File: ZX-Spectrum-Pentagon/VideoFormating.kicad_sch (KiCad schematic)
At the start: 10 parts

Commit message: prepare for pcb
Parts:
- RVF1: value (none) -> 4.7kOm; footprint (none) -> Resistor_SMD:R_0805_2012Metric_Pad1.20x1.40mm_HandSolder
- SWIO2: value (none) -> SW_Push_DPDT; footprint (none) -> Button_Switch_THT:SW_E-Switch_EG2219_DPDT_Angled
- U35, U36, U40: value (none) -> 74HC574; footprint (none) -> Package_DIP:DIP-20_W7.62mm
- U37, U38: value (none) -> 74HC153; footprint (none) -> Package_DIP:DIP-16_W7.62mm
- U39: value (none) -> GAL16V8; footprint (none) -> Package_DIP:DIP-20_W7.62mm
- U41: value (none) -> 74HC166; footprint (none) -> Package_DIP:DIP-16_W7.62mm
- U9: value (none) -> 74HC86; footprint (none) -> Package_DIP:DIP-14_W7.62mm
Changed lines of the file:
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@@
     (in_bom yes) (on_board yes)
     (property "Reference" "U35" (id 0) (at 55.88 24.13 0))
-    (property "Value" "" (id 1) (at 55.88 52.07 0))
-    (property "Footprint" "" (id 2) (at 55.88 45.72 0)
+    (property "Value" "74HC574" (id 1) (at 55.88 52.07 0))
+    (property "Footprint" "Package_DIP:DIP-20_W7.62mm" (id 2) (at 55.88 45.72 0)
       (effects (font (size 1.27 1.27)) hide)
     )
@@
     (in_bom yes) (on_board yes)
     (property "Reference" "U36" (id 0) (at 78.74 26.67 0))
-    (property "Value" "" (id 1) (at 78.74 54.61 0))
-    (property "Footprint" "" (id 2) (at 78.74 48.26 0)
+    (property "Value" "74HC574" (id 1) (at 78.74 54.61 0))
+    (property "Footprint" "Package_DIP:DIP-20_W7.62mm" (id 2) (at 78.74 48.26 0)
       (effects (font (size 1.27 1.27)) hide)
     )
@@
     (in_bom yes) (on_board yes)
     (property "Reference" "U40" (id 0) (at 55.88 153.67 0))
-    (property "Value" "" (id 1) (at 55.88 181.61 0))
-    (property "Footprint" "" (id 2) (at 55.88 175.26 0)
+    (property "Value" "74HC574" (id 1) (at 55.88 181.61 0))
+    (property "Footprint" "Package_DIP:DIP-20_W7.62mm" (id 2) (at 55.88 175.26 0)
       (effects (font (size 1.27 1.27)) hide)
     )
@@
     (in_bom yes) (on_board yes)
     (property "Reference" "U41" (id 0) (at 82.55 151.13 0))
-    (property "Value" "" (id 1) (at 82.55 186.69 0))
-    (property "Footprint" "" (id 2) (at 82.55 184.15 0)
+    (property "Value" "74HC166" (id 1) (at 82.55 186.69 0))
+    (property "Footprint" "Package_DIP:DIP-16_W7.62mm" (id 2) (at 82.55 184.15 0)
       (effects (font (size 1.27 1.27)) hide)
     )
@@
     (in_bom yes) (on_board yes)
     (property "Reference" "U37" (id 0) (at 135.89 26.67 0))
-    (property "Value" "" (id 1) (at 135.89 59.69 0))
-    (property "Footprint" "" (id 2) (at 135.89 41.91 0)
+    (property "Value" "74HC153" (id 1) (at 135.89 59.69 0))
+    (property "Footprint" "Package_DIP:DIP-16_W7.62mm" (id 2) (at 135.89 41.91 0)
       (effects (font (size 1.27 1.27)) hide)
     )
@@
     (in_bom yes) (on_board yes)
     (property "Reference" "U38" (id 0) (at 135.89 72.39 0))
-    (property "Value" "" (id 1) (at 135.89 105.41 0))
-    (property "Footprint" "" (id 2) (at 135.89 87.63 0)
+    (property "Value" "74HC153" (id 1) (at 135.89 105.41 0))
+    (property "Footprint" "Package_DIP:DIP-16_W7.62mm" (id 2) (at 135.89 87.63 0)
       (effects (font (size 1.27 1.27)) hide)
     )
@@
     (in_bom yes) (on_board yes)
     (property "Reference" "U39" (id 0) (at 83.82 95.25 0))
-    (property "Value" "" (id 1) (at 83.82 123.19 0))
-    (property "Footprint" "" (id 2) (at 83.82 95.25 0)
+    (property "Value" "GAL16V8" (id 1) (at 83.82 123.19 0))
+    (property "Footprint" "Package_DIP:DIP-20_W7.62mm" (id 2) (at 83.82 95.25 0)
       (effects (font (size 1.27 1.27)) hide)
     )
@@
     (in_bom yes) (on_board yes)
     (property "Reference" "SWIO2" (id 0) (at 114.3 156.21 0))
-    (property "Value" "" (id 1) (at 114.3 156.3624 0)
-      (effects (font (size 1.27 1.27)) hide)
-    )
-    (property "Footprint" "" (id 2) (at 114.3 161.29 0)
+    (property "Value" "SW_Push_DPDT" (id 1) (at 114.3 156.3624 0)
+      (effects (font (size 1.27 1.27)) hide)
+    )
+    (property "Footprint" "Button_Switch_THT:SW_E-Switch_EG2219_DPDT_Angled" (id 2) (at 114.3 161.29 0)
       (effects (font (size 1.27 1.27)) hide)
     )
@@
       (effects (font (size 1.27 1.27)) (justify left))
     )
-    (property "Value" "" (id 1) (at 97.79 157.48 0)
+    (property "Value" "4.7kOm" (id 1) (at 97.79 157.48 0)
       (effects (font (size 1.27 1.27)) (justify left))
     )
-    (property "Footprint" "" (id 2) (at 104.902 153.67 90)
+    (property "Footprint" "Resistor_SMD:R_0805_2012Metric_Pad1.20x1.40mm_HandSolder" (id 2) (at 104.902 153.67 90)
       (effects (font (size 1.27 1.27)) hide)
     )
@@
     (in_bom yes) (on_board yes)
     (property "Reference" "U9" (id 0) (at 137.16 133.35 0))
-    (property "Value" "" (id 1) (at 137.16 140.97 0))
-    (property "Footprint" "" (id 2) (at 137.16 144.78 0)
-      (effects (font (size 1.27 1.27)) hide)
-    )
+    (property "Value" "74HC86" (id 1) (at 137.16 140.97 0))
+    (property "Footprint" "Package_DIP:DIP-14_W7.62mm" (id 2) (at 137.16 144.78 0)
+      (effects (font (size 1.27 1.27)) hide)
+    )

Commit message: clear annotate
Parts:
- renumbered RVF1 to RVF?, SWIO2 to SWIO?, U35 to U?, U36 to U?, U40 to U?, U41 to U?, U37 to U?, U38 to U?, U39 to U?, U9 to U?
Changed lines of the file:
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@@
   (symbol (lib_id "74IEC:74HC574") (at 55.88 38.1 0) (unit 1)
     (in_bom yes) (on_board yes)
-    (property "Reference" "U35" (id 0) (at 55.88 24.13 0))
+    (property "Reference" "U?" (id 0) (at 55.88 24.13 0))
     (property "Value" "74HC574" (id 1) (at 55.88 52.07 0))
     (property "Footprint" "Package_DIP:DIP-20_W7.62mm" (id 2) (at 55.88 45.72 0)
@@
   (symbol (lib_id "74IEC:74HC574") (at 78.74 40.64 0) (unit 1)
     (in_bom yes) (on_board yes)
-    (property "Reference" "U36" (id 0) (at 78.74 26.67 0))
+    (property "Reference" "U?" (id 0) (at 78.74 26.67 0))
     (property "Value" "74HC574" (id 1) (at 78.74 54.61 0))
     (property "Footprint" "Package_DIP:DIP-20_W7.62mm" (id 2) (at 78.74 48.26 0)
@@
   (symbol (lib_id "power:GND") (at 68.58 57.15 0) (unit 1)
     (in_bom yes) (on_board yes)
-    (property "Reference" "#PWR0157" (id 0) (at 68.58 63.5 0)
+    (property "Reference" "#PWR?" (id 0) (at 68.58 63.5 0)
       (effects (font (size 1.27 1.27)) hide)
     )
@@
   (symbol (lib_id "74IEC:74HC574") (at 55.88 167.64 0) (unit 1)
     (in_bom yes) (on_board yes)
-    (property "Reference" "U40" (id 0) (at 55.88 153.67 0))
+    (property "Reference" "U?" (id 0) (at 55.88 153.67 0))
     (property "Value" "74HC574" (id 1) (at 55.88 181.61 0))
     (property "Footprint" "Package_DIP:DIP-20_W7.62mm" (id 2) (at 55.88 175.26 0)
@@
   (symbol (lib_id "74IEC:74HC166") (at 82.55 168.91 0) (unit 1)
     (in_bom yes) (on_board yes)
-    (property "Reference" "U41" (id 0) (at 82.55 151.13 0))
+    (property "Reference" "U?" (id 0) (at 82.55 151.13 0))
     (property "Value" "74HC166" (id 1) (at 82.55 186.69 0))
     (property "Footprint" "Package_DIP:DIP-16_W7.62mm" (id 2) (at 82.55 184.15 0)
@@
   (symbol (lib_id "power:GND") (at 71.12 186.69 0) (unit 1)
     (in_bom yes) (on_board yes)
-    (property "Reference" "#PWR0155" (id 0) (at 71.12 193.04 0)
+    (property "Reference" "#PWR?" (id 0) (at 71.12 193.04 0)
       (effects (font (size 1.27 1.27)) hide)
     )
@@
   (symbol (lib_id "74IEC:74XX153") (at 135.89 43.18 0) (unit 1)
     (in_bom yes) (on_board yes)
-    (property "Reference" "U37" (id 0) (at 135.89 26.67 0))
+    (property "Reference" "U?" (id 0) (at 135.89 26.67 0))
     (property "Value" "74HC153" (id 1) (at 135.89 59.69 0))
     (property "Footprint" "Package_DIP:DIP-16_W7.62mm" (id 2) (at 135.89 41.91 0)
@@
   (symbol (lib_id "74IEC:74XX153") (at 135.89 88.9 0) (unit 1)
     (in_bom yes) (on_board yes)
-    (property "Reference" "U38" (id 0) (at 135.89 72.39 0))
+    (property "Reference" "U?" (id 0) (at 135.89 72.39 0))
     (property "Value" "74HC153" (id 1) (at 135.89 105.41 0))
     (property "Footprint" "Package_DIP:DIP-16_W7.62mm" (id 2) (at 135.89 87.63 0)
@@
   (symbol (lib_id "power:GND") (at 124.46 125.73 0) (unit 1)
     (in_bom yes) (on_board yes)
-    (property "Reference" "#PWR0151" (id 0) (at 124.46 132.08 0)
+    (property "Reference" "#PWR?" (id 0) (at 124.46 132.08 0)
       (effects (font (size 1.27 1.27)) hide)
     )
@@
   (symbol (lib_id "Gal:GAL16V8") (at 83.82 109.22 0) (unit 1)
     (in_bom yes) (on_board yes)
-    (property "Reference" "U39" (id 0) (at 83.82 95.25 0))
+    (property "Reference" "U?" (id 0) (at 83.82 95.25 0))
     (property "Value" "GAL16V8" (id 1) (at 83.82 123.19 0))
     (property "Footprint" "Package_DIP:DIP-20_W7.62mm" (id 2) (at 83.82 95.25 0)
@@
   (symbol (lib_id "Switch:SW_Push_DPDT") (at 114.3 166.37 0) (unit 1)
     (in_bom yes) (on_board yes)
-    (property "Reference" "SWIO2" (id 0) (at 114.3 156.21 0))
+    (property "Reference" "SWIO?" (id 0) (at 114.3 156.21 0))
     (property "Value" "SW_Push_DPDT" (id 1) (at 114.3 156.3624 0)
       (effects (font (size 1.27 1.27)) hide)
@@
   (symbol (lib_id "power:GND") (at 123.19 176.53 0) (mirror y) (unit 1)
     (in_bom yes) (on_board yes)
-    (property "Reference" "#PWR0152" (id 0) (at 123.19 182.88 0)
+    (property "Reference" "#PWR?" (id 0) (at 123.19 182.88 0)
       (effects (font (size 1.27 1.27)) hide)
     )
@@
   (symbol (lib_id "Device:R") (at 106.68 153.67 0) (unit 1)
     (in_bom yes) (on_board yes)
-    (property "Reference" "RVF1" (id 0) (at 99.06 151.13 0)
+    (property "Reference" "RVF?" (id 0) (at 99.06 151.13 0)
       (effects (font (size 1.27 1.27)) (justify left))
     )
@@
   (symbol (lib_id "power:VCC") (at 106.68 144.78 0) (unit 1)
     (in_bom yes) (on_board yes)
-    (property "Reference" "#PWR0153" (id 0) (at 106.68 148.59 0)
+    (property "Reference" "#PWR?" (id 0) (at 106.68 148.59 0)
       (effects (font (size 1.27 1.27)) hide)
     )
@@
   (symbol (lib_id "74IEC:74HC86") (at 137.16 137.16 0) (unit 4)
     (in_bom yes) (on_board yes)
-    (property "Reference" "U9" (id 0) (at 137.16 133.35 0))
+    (property "Reference" "U?" (id 0) (at 137.16 133.35 0))
     (property "Value" "74HC86" (id 1) (at 137.16 140.97 0))
     (property "Footprint" "Package_DIP:DIP-14_W7.62mm" (id 2) (at 137.16 144.78 0)
@@
   (symbol (lib_id "power:VCC") (at 67.31 120.65 90) (unit 1)
     (in_bom yes) (on_board yes)
-    (property "Reference" "#PWR0156" (id 0) (at 71.12 120.65 0)
-      (effects (font (size 1.27 1.27)) hide)
-    )
+    (property "Reference" "#PWR?" (id 0) (at 71.12 120.65 0)
+      (effects (font (size 1.27 1.27)) hide)
+    )

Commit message: new footprint for button
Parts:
- SWIO?: footprint Button_Switch_THT:SW_E-Switch_EG2219_DPDT_Angled -> ZX-Spectrum-Pentagon:PS-22F03
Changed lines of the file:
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@@
       (effects (font (size 1.27 1.27)) hide)
     )
-    (property "Footprint" "Button_Switch_THT:SW_E-Switch_EG2219_DPDT_Angled" (id 2) (at 114.3 161.29 0)
+    (property "Footprint" "ZX-Spectrum-Pentagon:PS-22F03" (id 2) (at 114.3 161.29 0)
       (effects (font (size 1.27 1.27)) hide)
     )

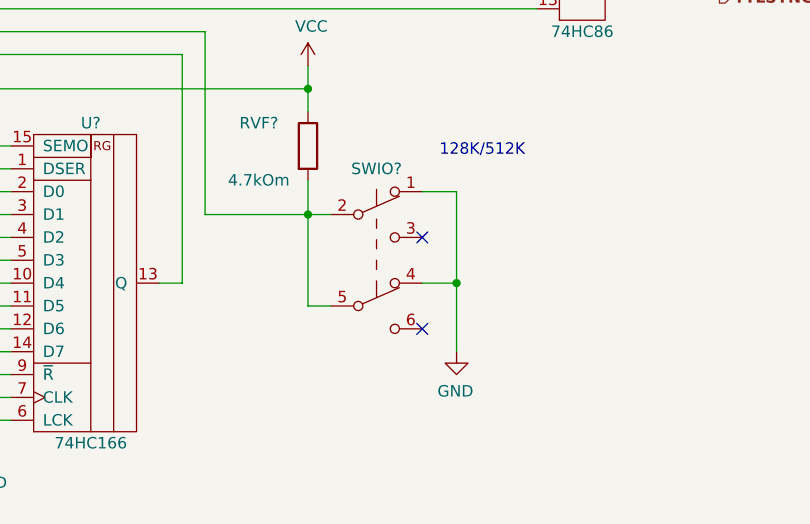
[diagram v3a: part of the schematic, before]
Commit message: use new symbol for switch button
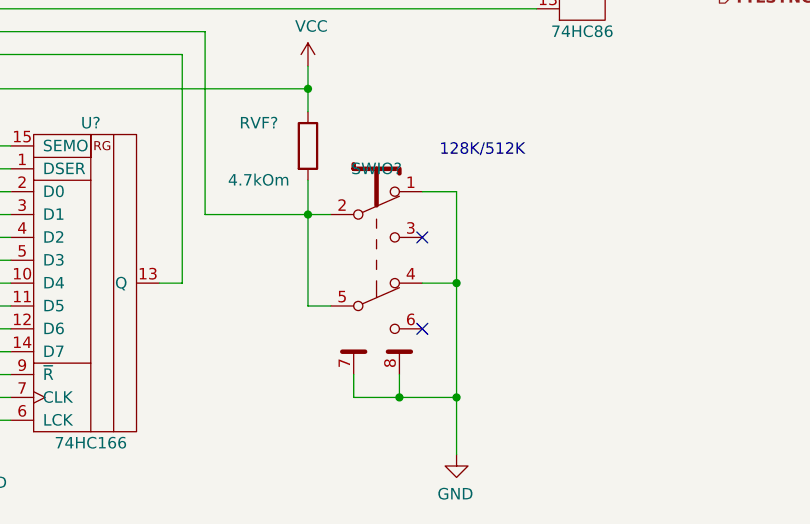
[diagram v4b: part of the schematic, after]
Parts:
- SWIO?: symbol Switch:SW_Push_DPDT -> zx_custom_symbol:SW_Push_DPDT
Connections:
- net GND: now also SWIO?.7, SWIO?.8
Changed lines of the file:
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@@
   (junction (at 119.38 100.33) (diameter 0) (color 0 0 0 0)
   )
+  (junction (at 123.19 181.61) (diameter 0) (color 0 0 0 0)
+  )
   (junction (at 71.12 184.15) (diameter 0) (color 0 0 0 0)
   )
@@
   )
   (junction (at 124.46 97.79) (diameter 0) (color 0 0 0 0)
+  )
+  (junction (at 116.84 181.61) (diameter 0) (color 0 0 0 0)
   )
   (junction (at 124.46 41.91) (diameter 0) (color 0 0 0 0)
@@
     (stroke (width 0) (type default) (color 0 0 0 0))
   )
-  (wire (pts (xy 123.19 168.91) (xy 123.19 176.53))
+  (wire (pts (xy 123.19 168.91) (xy 123.19 181.61))
     (stroke (width 0) (type default) (color 0 0 0 0))
   )
@@
     (stroke (width 0) (type default) (color 0 0 0 0))
   )
+  (wire (pts (xy 123.19 181.61) (xy 123.19 187.96))
+    (stroke (width 0) (type default) (color 0 0 0 0))
+  )
   (wire (pts (xy 66.04 57.15) (xy 40.64 57.15))
     (stroke (width 0) (type default) (color 0 0 0 0))
@@
     (stroke (width 0) (type default) (color 0 0 0 0))
   )
+  (wire (pts (xy 111.76 179.07) (xy 111.76 181.61))
+    (stroke (width 0) (type default) (color 0 0 0 0))
+  )
   (wire (pts (xy 25.4 41.91) (xy 35.56 41.91))
     (stroke (width 0) (type default) (color 0 0 0 0))
@@
     (stroke (width 0) (type default) (color 0 0 0 0))
   )
+  (wire (pts (xy 116.84 179.07) (xy 116.84 181.61))
+    (stroke (width 0) (type default) (color 0 0 0 0))
+  )
   (bus (pts (xy 38.1 138.43) (xy 38.1 140.97))
     (stroke (width 0) (type default) (color 0 0 0 0))
@@
     (stroke (width 0) (type default) (color 0 0 0 0))
   )
+  (wire (pts (xy 111.76 181.61) (xy 116.84 181.61))
+    (stroke (width 0) (type default) (color 0 0 0 0))
+  )
   (wire (pts (xy 116.84 52.07) (xy 116.84 67.31))
     (stroke (width 0) (type default) (color 0 0 0 0))
@@
   )
   (wire (pts (xy 63.5 176.53) (xy 73.66 176.53))
+    (stroke (width 0) (type default) (color 0 0 0 0))
+  )
+  (wire (pts (xy 116.84 181.61) (xy 123.19 181.61))
     (stroke (width 0) (type default) (color 0 0 0 0))
   )
@@
     (pin "9")
   )
-  (symbol (lib_id "Switch:SW_Push_DPDT") (at 114.3 166.37 0) (unit 1)
+  (symbol (lib_id "zx_custom_symbol:SW_Push_DPDT") (at 114.3 166.37 0) (unit 1)
     (in_bom yes) (on_board yes)
     (property "Reference" "SWIO?" (id 0) (at 114.3 156.21 0))
@@
       (effects (font (size 1.27 1.27)) hide)
     )
-    (property "Footprint" "ZX-Spectrum-Pentagon:PS-22F03" (id 2) (at 114.3 161.29 0)
-      (effects (font (size 1.27 1.27)) hide)
-    )
-    (property "Datasheet" "~" (id 3) (at 114.3 161.29 0)
+    (property "Footprint" "ZX-Spectrum-Pentagon:PS-22F03" (id 2) (at 114.3 166.37 0)
+      (effects (font (size 1.27 1.27)) hide)
+    )
+    (property "Datasheet" "~" (id 3) (at 114.3 166.37 0)
       (effects (font (size 1.27 1.27)) hide)
     )
@@
     (pin "5")
     (pin "6")
-  )
-  (symbol (lib_id "power:GND") (at 123.19 176.53 0) (mirror y) (unit 1)
+    (pin "7")
+    (pin "8")
+  )
+  (symbol (lib_id "power:GND") (at 123.19 187.96 0) (mirror y) (unit 1)
     (in_bom yes) (on_board yes)
-    (property "Reference" "#PWR?" (id 0) (at 123.19 182.88 0)
-      (effects (font (size 1.27 1.27)) hide)
-    )
-    (property "Value" "GND" (id 1) (at 123.063 180.9242 0))
-    (property "Footprint" "" (id 2) (at 123.19 176.53 0)
-      (effects (font (size 1.27 1.27)) hide)
-    )
-    (property "Datasheet" "" (id 3) (at 123.19 176.53 0)
-      (effects (font (size 1.27 1.27)) hide)
-    )
+    (property "Reference" "#PWR?" (id 0) (at 123.19 194.31 0)
+      (effects (font (size 1.27 1.27)) hide)
+    )
+    (property "Value" "GND" (id 1) (at 123.063 192.3542 0))
+    (property "Footprint" "" (id 2) (at 123.19 187.96 0)
+      (effects (font (size 1.27 1.27)) hide)
+    )
+    (property "Datasheet" "" (id 3) (at 123.19 187.96 0)
+      (effects (font (size 1.27 1.27)) hide)
+    )

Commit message: rename companent
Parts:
- SWVF?: renamed from SWIO?; value SW_Push_DPDT -> (none); footprint ZX-Spectrum-Pentagon:PS-22F03 -> (none)
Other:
- note removed: "128K/512K"
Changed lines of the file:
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@@
     (stroke (width 0) (type default) (color 0 0 0 0))
-  )
-  (text "128K/512K" (at 130.81 154.94 180)
-    (effects (font (size 1.27 1.27)) (justify right bottom))
   )
   (label "MD3" (at 40.64 34.29 0)
@@
   (symbol (lib_id "zx_custom_symbol:SW_Push_DPDT") (at 114.3 166.37 0) (unit 1)
     (in_bom yes) (on_board yes)
-    (property "Reference" "SWIO?" (id 0) (at 114.3 156.21 0))
-    (property "Value" "SW_Push_DPDT" (id 1) (at 114.3 156.3624 0)
-      (effects (font (size 1.27 1.27)) hide)
-    )
-    (property "Footprint" "ZX-Spectrum-Pentagon:PS-22F03" (id 2) (at 114.3 166.37 0)
-      (effects (font (size 1.27 1.27)) hide)
-    )
+    (property "Reference" "SWVF?" (id 0) (at 114.3 153.67 0))
+    (property "Value" "" (id 1) (at 114.3 184.15 0))
+    (property "Footprint" "" (id 2) (at 114.3 166.37 0)
+      (effects (font (size 1.27 1.27)) hide)
+    )

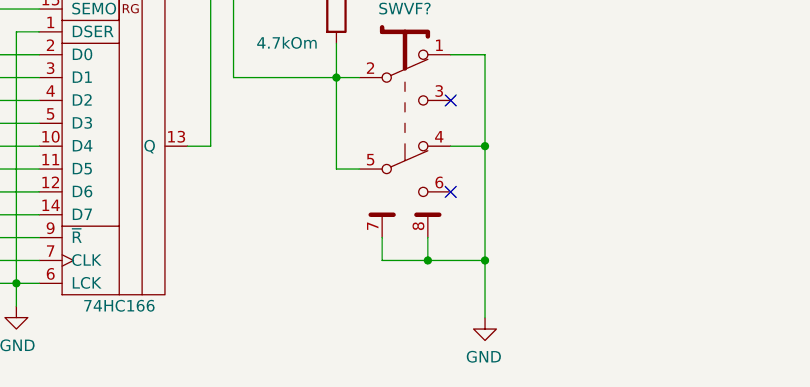
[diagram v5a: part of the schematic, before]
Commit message: revert data bus HC245 delete invertor for another direction fix line label
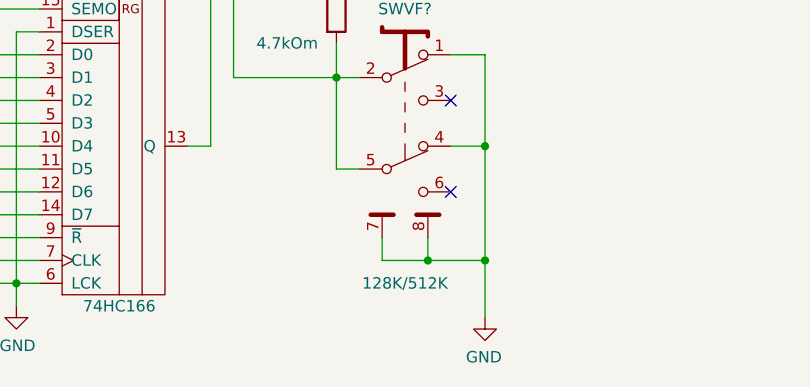
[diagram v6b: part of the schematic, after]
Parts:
- SWVF?: value (none) -> 128K/512K; footprint (none) -> ZX-Spectrum-Pentagon:PS-22F03
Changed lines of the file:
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@@
     (in_bom yes) (on_board yes)
     (property "Reference" "SWVF?" (id 0) (at 114.3 153.67 0))
-    (property "Value" "" (id 1) (at 114.3 184.15 0))
-    (property "Footprint" "" (id 2) (at 114.3 166.37 0)
+    (property "Value" "128K/512K" (id 1) (at 114.3 184.15 0))
+    (property "Footprint" "ZX-Spectrum-Pentagon:PS-22F03" (id 2) (at 114.3 166.37 0)
       (effects (font (size 1.27 1.27)) hide)
     )
